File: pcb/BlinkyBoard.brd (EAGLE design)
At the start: 25.2 x 10 mm, 27 parts, among them Q1 16 MHz

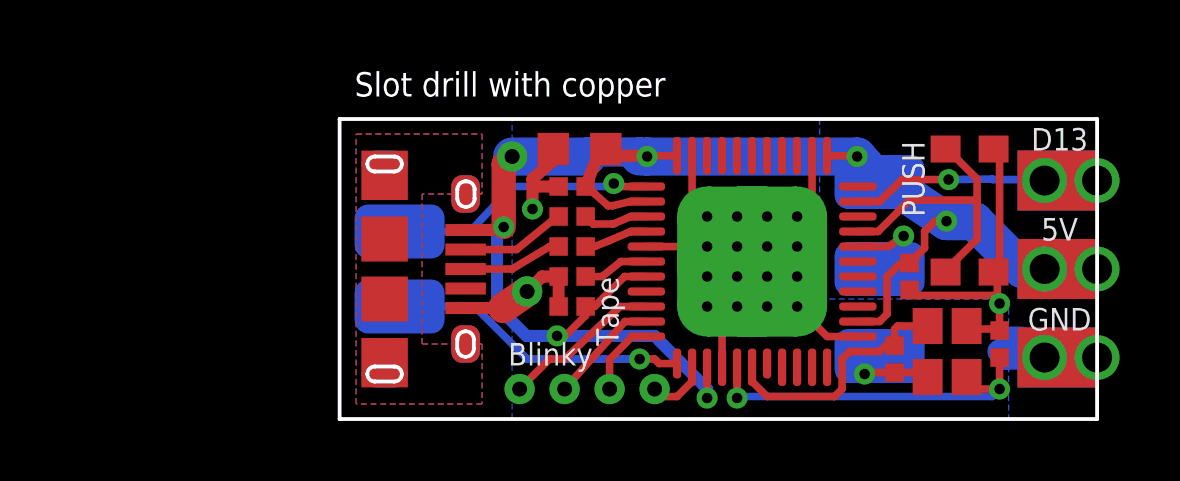
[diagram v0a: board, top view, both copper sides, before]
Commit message: RevF release: modify pads to support WS2811B
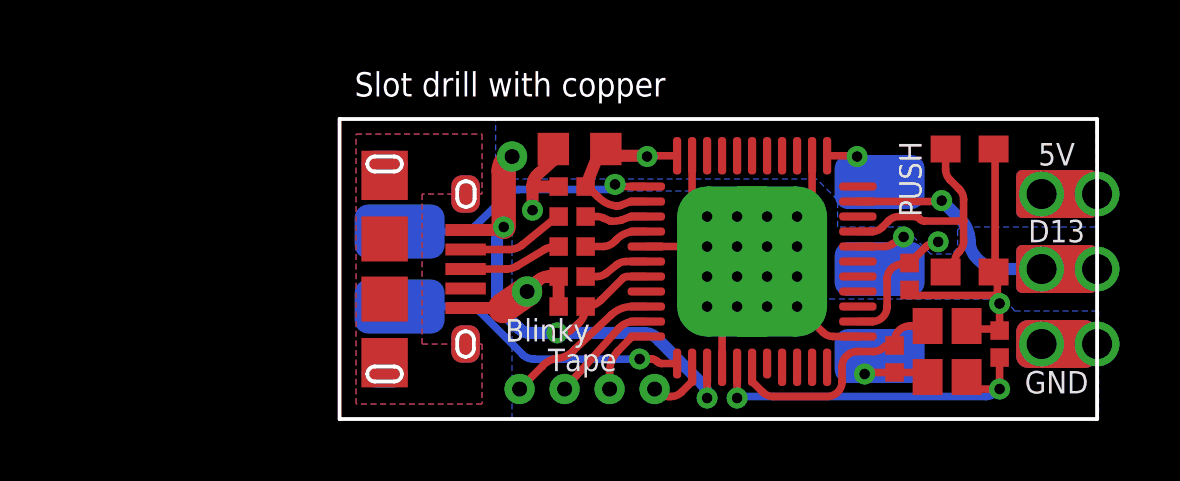
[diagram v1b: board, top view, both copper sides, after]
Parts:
- removed WS1, WS3: WS2811_CONNECTORSTRIP, blinkiverse:WS2811_CONNECTOR
- added U$9: WS2812B_CONNECTOR, blinkiverse:WS2812B_CONNECTOR
- moved U$15 0.36 mm to (20.9, 6.70)
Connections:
- net D13: now also U$9.DATA, U$9.DATA1, U$9.DATA_1, U$9.DATA_2; no longer WS1.DATA, WS3.DATA
- net GND: now also U$9.GND, U$9.GND1, U$9.GND_1, U$9.GND_2; no longer WS1.GND, WS3.GND
- net VCC: now also U$9.5V, U$9.5V1, U$9.5V_1, U$9.5V_2; no longer WS1.5V, WS3.5V
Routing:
- net VCC: track 54.6 -> 31.2 mm, vias 8 -> 6
- net GND: track 36.4 -> 31.6 mm, vias 5 -> 3
- net D10: track 9.68 -> 8.51 mm
- net D13: track 8.99 -> 9.69 mm, vias 3 -> 1
- net N$9: track 8.41 -> 7.81 mm
- added copper zone on layer 16, net VCC
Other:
- board text added: "8/2013"
- board text added: "Rev F"
- board text removed: "7/13"
- board text removed: "Rev E"

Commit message: Flip gnd/5v to match WS2812B strip.
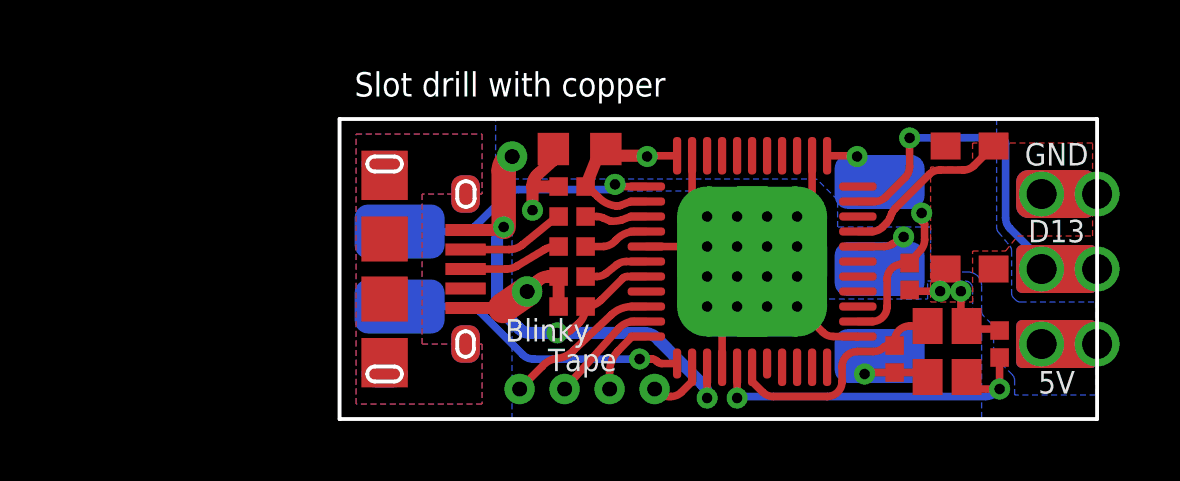
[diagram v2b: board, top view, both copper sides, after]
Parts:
- S1: device blinkyboard:GLOWBOARD_KMR211G_SWITCH -> blinkiverse:GLOWBOARD_KMR211G_SWITCH
- turned S1 to 90 degrees
- flipped U$9 to the bottom, turned to 180 degrees
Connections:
- net D10: no longer S1.P$3
- net GND: no longer S1.P$2
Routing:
- net GND: track 31.6 -> 24.7 mm, vias 3 -> 4
- net D13: track 9.69 -> 13.0 mm
- net D10: track 8.51 -> 5.69 mm
- net VCC: track 31.2 -> 31.9 mm
- added copper zone on layer 1, net GND
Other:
- board text added: "Rev G"
- board text removed: "PUSH"
- board text removed: "Rev F"

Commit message: Silkscreen fix: Analog is on A9, not A11!
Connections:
- net A10 renamed A9
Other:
- board text added: "A9"
- board text removed: "A11"
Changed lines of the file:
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@@
 <?xml version="1.0" encoding="utf-8"?>
 <!DOCTYPE eagle SYSTEM "eagle.dtd">
-<eagle version="6.5.0">
+<eagle version="6.4">
 <drawing>
 <settings>
@@
 <text x="23.9" y="5.89" size="0.75" layer="26" font="vector" ratio="15" rot="MR0" align="bottom-center">D13</text>
 <text x="23.9" y="8.45" size="0.75" layer="26" font="vector" ratio="15" rot="MR0" align="bottom-center">GND</text>
-<text x="20.5" y="8.75" size="0.75" layer="26" font="vector" ratio="15" rot="MR0" align="bottom-center">5V</text>
+<text x="20.3" y="8.75" size="0.75" layer="26" font="vector" ratio="15" rot="MR0" align="bottom-center">5V</text>
 <text x="20.75" y="2" size="0.75" layer="26" font="vector" ratio="15" rot="MR0" align="center">GND</text>
-<text x="20.5" y="8.75" size="0.75" layer="26" font="vector" ratio="15" rot="MR0" align="bottom-center">5V</text>
-<text x="20.75" y="5" size="0.75" layer="26" font="vector" ratio="15" rot="MR0" align="center">A11</text>
+<text x="20.35" y="5" size="0.75" layer="26" font="vector" ratio="15" rot="MR0" align="center">A9</text>
 <text x="4.35" y="6.25" size="0.75" layer="26" font="vector" ratio="15" rot="MR0" align="center">D7</text>
 <text x="4.65" y="3.75" size="0.75" layer="26" font="vector" ratio="15" rot="MR0" align="center">D11</text>
@@
 <wire x1="9.14" y1="7.75" x2="10.225" y2="7.75" width="0.254" layer="1"/>
 </signal>
-<signal name="A10">
+<signal name="A9">
 <contactref element="U$2" pad="29"/>
 <via x="18.8" y="6.07" extent="1-16" drill="0.35"/>
@@
 </signal>
 </signals>
-<errors>
-</errors>
 </board>
 </drawing>

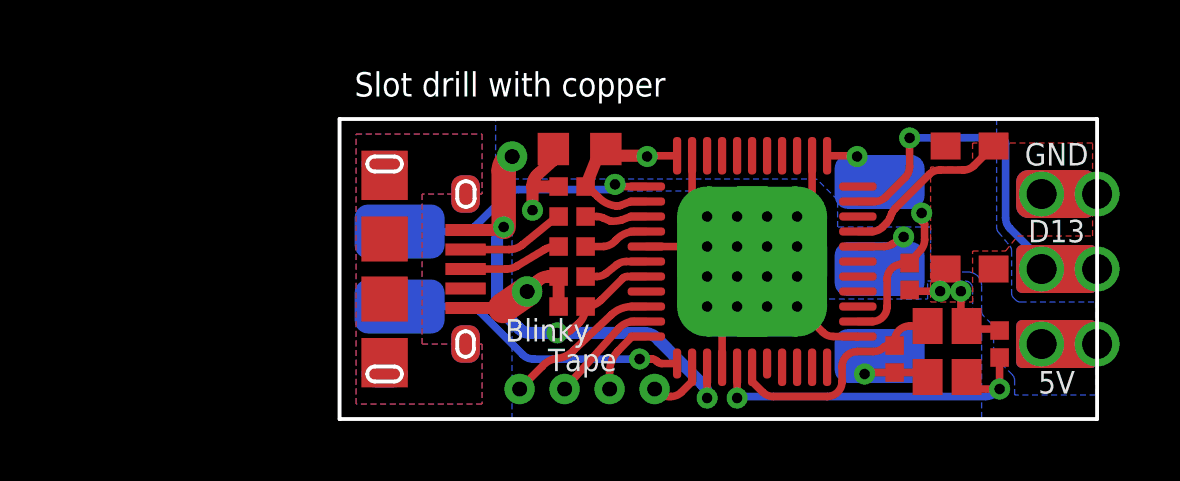
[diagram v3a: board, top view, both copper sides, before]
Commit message: Add series resistor to the output data line, so it can be removed from the flex strip
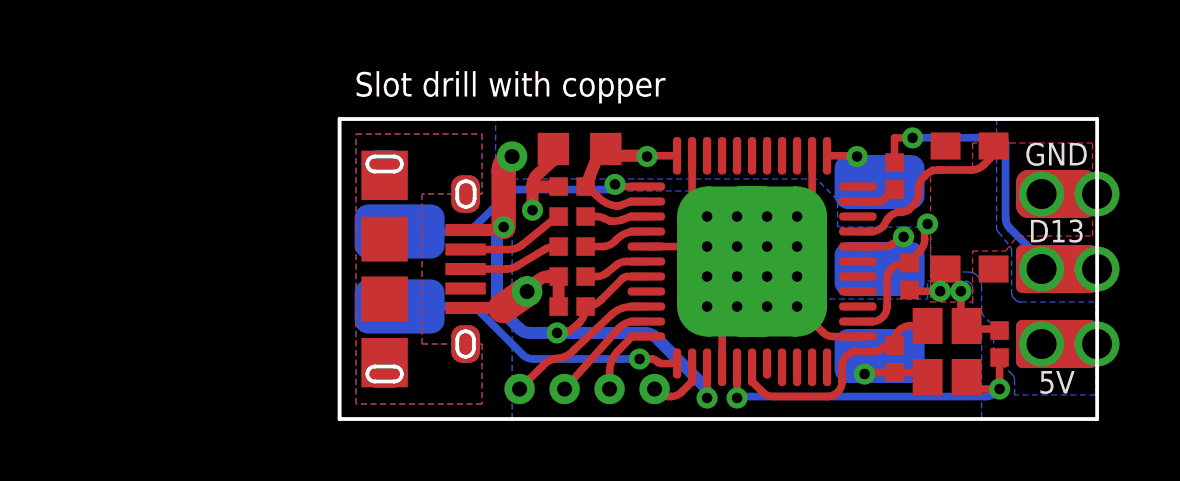
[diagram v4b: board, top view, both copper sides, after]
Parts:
- added R3: ??, blinkiverse:RES_0402_KEMET_MEDIAN
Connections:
- new net LED_DATA: R3.P$2, U$9.DATA, U$9.DATA1, U$9.DATA_1, U$9.DATA_2
- net D13: now also R3.P$1; no longer U$9.DATA, U$9.DATA1, U$9.DATA_1, U$9.DATA_2
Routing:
- net D13: track 13.0 -> 1.38 mm, vias 1 -> 0
- net LED_DATA: track 0.00 -> 10.8 mm, vias 0 -> 1
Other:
- board text added: "11/2013"
- board text added: "Rev H"
- board text added: "blinkinlabs.com"
- board text removed: "8/2013"
- board text removed: "Blinky"
- board text removed: "Rev G"
- board text removed: "Tape"
- board text removed: "blinkytape.com"
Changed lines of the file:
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@@
 <?xml version="1.0" encoding="utf-8"?>
 <!DOCTYPE eagle SYSTEM "eagle.dtd">
-<eagle version="6.4">
+<eagle version="6.5.0">
 <drawing>
 <settings>
@@
 <text x="9.15" y="6" size="1.016" layer="26" font="vector" ratio="20" rot="MR0" align="center">Blinky
 Tape</text>
-<text x="9.15" y="3.85" size="0.8128" layer="26" font="vector" ratio="20" rot="MR0" align="center">Rev G</text>
+<text x="9.15" y="3.85" size="0.8128" layer="26" font="vector" ratio="20" rot="MR0" align="center">Rev H</text>
 <text x="23.9" y="0.85" size="0.75" layer="25" font="vector" ratio="15" align="bottom-center">5V</text>
 <text x="23.9" y="5.89" size="0.75" layer="25" font="vector" ratio="15" align="bottom-center">D13</text>
 <text x="23.9" y="8.45" size="0.75" layer="25" font="vector" ratio="15" align="bottom-center">GND</text>
-<text x="8.09" y="1.97" size="0.75" layer="25" font="vector" ratio="15" align="center">Tape</text>
-<text x="11.24" y="2.6" size="0.9" layer="26" font="vector" ratio="20" rot="MR0" align="center">blinkytape.com</text>
+<text x="11.24" y="2.6" size="0.9" layer="26" font="vector" ratio="20" rot="MR0" align="center">blinkinlabs.com</text>
 <text x="23.9" y="0.85" size="0.75" layer="26" font="vector" ratio="15" rot="MR0" align="bottom-center">5V</text>
 <text x="23.9" y="5.89" size="0.75" layer="26" font="vector" ratio="15" rot="MR0" align="bottom-center">D13</text>
@@
 <text x="4.65" y="3.75" size="0.75" layer="26" font="vector" ratio="15" rot="MR0" align="center">D11</text>
 <text x="0.5" y="10.75" size="0.8128" layer="46">Slot drill with copper</text>
-<text x="13.75" y="8.75" size="0.75" layer="26" font="vector" ratio="15" rot="MR0" align="center">8/2013</text>
-<text x="6.93" y="2.96" size="0.75" layer="25" font="vector" ratio="15" align="center">Blinky</text>
+<text x="13.75" y="8.75" size="0.75" layer="26" font="vector" ratio="15" rot="MR0" align="center">11/2013</text>
 </plain>
 <attributes>
@@
 <element name="U$15" library="blinkiverse" package="OSHW-LOGO-S" value="" x="20.89" y="6.7" rot="MR0"/>
 <element name="U$9" library="blinkiverse" package="WS2812B_CONNECTOR" value="WS2812B_CONNECTOR" x="23.9" y="5" rot="MR180"/>
+<element name="R3" library="blinkiverse" package="RES_0402_KEMET_MEDIAN" value="??" x="18.5" y="8.1" rot="R90"/>
 </elements>
 <signals>
@@
 <contactref element="S1" pad="P$4"/>
 <contactref element="U$2" pad="30"/>
-<wire x1="17.275" y1="6.25" x2="17.74289375" y2="6.25" width="0.254" layer="1"/>
-<wire x1="17.74289375" y1="6.25" x2="18.096446875" y2="6.396446875" width="0.254" layer="1" curve="45"/>
-<wire x1="18.4033625" y1="6.8495375" x2="18.338059375" y2="6.691884375" width="0.254" layer="1"/>
-<wire x1="18.338059375" y1="6.691884375" x2="18.229675" y2="6.529675" width="0.254" layer="1" curve="-22.499569"/>
-<wire x1="18.229675" y1="6.529675" x2="18.096446875" y2="6.396446875" width="0.254" layer="1"/>
-<wire x1="19.653553125" y1="8.153553125" x2="18.511746875" y2="7.011746875" width="0.254" layer="1"/>
-<wire x1="18.511746875" y1="7.011746875" x2="18.4033625" y2="6.8495375" width="0.254" layer="1" curve="22.499685"/>
-<wire x1="19.653553125" y1="8.153553125" x2="20.00710625" y2="8.3" width="0.254" layer="1" curve="-45"/>
-<wire x1="20.00710625" y1="8.3" x2="20.79289375" y2="8.3" width="0.254" layer="1"/>
-<wire x1="20.79289375" y1="8.3" x2="21.146446875" y2="8.446446875" width="0.254" layer="1" curve="45"/>
-<wire x1="21.146446875" y1="8.446446875" x2="21.8" y2="9.1" width="0.254" layer="1"/>
+<wire x1="17.275" y1="6.25" x2="17.701471875" y2="6.25" width="0.254" layer="1"/>
+<wire x1="17.701471875" y1="6.25" x2="18.125734375" y2="6.425734375" width="0.254" layer="1" curve="44.999789"/>
+<wire x1="18.125734375" y1="6.425734375" x2="18.263603125" y2="6.663603125" width="0.254" layer="1"/>
+<wire x1="18.263603125" y1="6.663603125" x2="18.651471875" y2="6.9" width="0.254" layer="1" curve="-45"/>
+<wire x1="18.651471875" y1="6.9" x2="18.975734375" y2="6.975734375" width="0.254" layer="1" curve="44.999789"/>
+<wire x1="18.975734375" y1="6.975734375" x2="19.124265625" y2="7.124265625" width="0.254" layer="1"/>
+<wire x1="19.124265625" y1="7.124265625" x2="19.3" y2="7.548528125" width="0.254" layer="1" curve="44.999702"/>
+<wire x1="19.3" y1="7.548528125" x2="19.3" y2="7.651471875" width="0.254" layer="1"/>
+<wire x1="19.3" y1="7.651471875" x2="19.475734375" y2="8.075734375" width="0.254" layer="1" curve="-44.999789"/>
+<wire x1="19.475734375" y1="8.075734375" x2="19.524265625" y2="8.124265625" width="0.254" layer="1"/>
+<wire x1="19.524265625" y1="8.124265625" x2="19.948528125" y2="8.3" width="0.254" layer="1" curve="-44.999702"/>
+<wire x1="19.948528125" y1="8.3" x2="21.051471875" y2="8.3" width="0.254" layer="1"/>
+<wire x1="21.051471875" y1="8.3" x2="21.475734375" y2="8.475734375" width="0.254" layer="1" curve="44.999789"/>
+<wire x1="21.475734375" y1="8.475734375" x2="21.8" y2="8.8" width="0.254" layer="1"/>
+<wire x1="21.8" y1="8.8" x2="21.8" y2="9.1" width="0.254" layer="1"/>
 </signal>
 <signal name="AREF">
@@
 <wire x1="9.550390625" y1="5.25" x2="10.225" y2="5.25" width="0.254" layer="1"/>
 </signal>
-<signal name="D13">
-<contactref element="U$2" pad="32"/>
+<signal name="LED_DATA">
+<via x="19.1" y="9.37" extent="1-16" drill="0.35"/>
+<wire x1="19.1" y1="9.37" x2="22" y2="9.38" width="0.254" layer="16"/>
+<wire x1="22" y1="9.38" x2="22.2" y2="9.18" width="0.254" layer="16" curve="-90"/>
+<wire x1="22.2" y1="9.18" x2="22.2" y2="6.70710625" width="0.254" layer="16"/>
+<wire x1="22.2" y1="6.70710625" x2="22.346446875" y2="6.353553125" width="0.254" layer="16" curve="45"/>
+<wire x1="22.346446875" y1="6.353553125" x2="23.4" y2="5.3" width="0.254" layer="16"/>
 <contactref element="U$9" pad="DATA1"/>
 <contactref element="U$9" pad="DATA_1"/>
 <contactref element="U$9" pad="DATA_2"/>
 <contactref element="U$9" pad="DATA"/>
+<contactref element="R3" pad="P$2"/>
 <wire x1="25.25" y1="5" x2="23.9" y2="5" width="0.4064" layer="16"/>
 <wire x1="23.4" y1="5" x2="23.9" y2="5" width="0.4064" layer="16"/>
-<wire x1="17.275" y1="7.25" x2="17.84289375" y2="7.25" width="0.254" layer="1"/>
-<wire x1="17.84289375" y1="7.25" x2="18.196446875" y2="7.396446875" width="0.254" layer="1" curve="45"/>
-<wire x1="18.196446875" y1="7.396446875" x2="18.853553125" y2="8.053553125" width="0.254" layer="1"/>
-<wire x1="18.853553125" y1="8.053553125" x2="19" y2="8.40710625" width="0.254" layer="1" curve="45"/>
-<wire x1="19" y1="8.40710625" x2="19" y2="9.37" width="0.254" layer="1"/>
-<via x="19" y="9.37" extent="1-16" drill="0.35"/>
-<wire x1="19" y1="9.37" x2="22" y2="9.38" width="0.254" layer="16"/>
-<wire x1="22" y1="9.38" x2="22.2" y2="9.18" width="0.254" layer="16" curve="-90"/>
-<wire x1="22.2" y1="9.18" x2="22.2" y2="6.70710625" width="0.254" layer="16"/>
-<wire x1="22.2" y1="6.70710625" x2="22.346446875" y2="6.353553125" width="0.254" layer="16" curve="45"/>
-<wire x1="22.346446875" y1="6.353553125" x2="23.4" y2="5.3" width="0.254" layer="16"/>
-<wire x1="23.4" y1="5.3" x2="23.4" y2="5" width="0.254" layer="16"/>
+<wire x1="19.1" y1="9.37" x2="18.5" y2="9.37" width="0.254" layer="1"/>
+<wire x1="18.5" y1="9.37" x2="18.5" y2="8.55" width="0.254" layer="1"/>
 <wire x1="23.9" y1="5" x2="23.9" y2="5" width="0" layer="19" extent="1-16"/>
+<wire x1="23.4" y1="5.3" x2="23.4" y2="5" width="0" layer="19" extent="16-16"/>
 </signal>
 <signal name="VCC">
@@
 <wire x1="5.05" y1="6.3" x2="5.47" y2="6.4" width="0.4" layer="1"/>
 <contactref element="U$12" pad="P$1"/>
-<via x="19.40076875" y="6.866153125" extent="1-16" drill="0.35"/>
+<via x="19.6" y="6.5" extent="1-16" drill="0.35"/>
 <wire x1="8.2" y1="3.75" x2="7.984815625" y2="3.200965625" width="0.254" layer="1" curve="-45.83031"/>
 <wire x1="7.984815625" y1="3.200965625" x2="7.67931875" y2="2.944196875" width="0.254" layer="1"/>
@@
 <wire x1="19.38198125" y1="5.65063125" x2="19.50056875" y2="5.975284375" width="0.254" layer="1" curve="40.441105"/>
 <wire x1="19.50056875" y1="5.975284375" x2="19.5" y2="6.5" width="0.254" layer="1"/>
-<wire x1="19.5" y1="6.5" x2="19.40076875" y2="6.59923125" width="0.254" layer="1"/>
-<wire x1="19.40076875" y1="6.59923125" x2="19.40076875" y2="6.866153125" width="0.254" layer="1"/>
+<wire x1="19.6" y1="6.5" x2="19.5" y2="6.5" width="0.254" layer="1"/>
 <wire x1="23.9" y1="2.5" x2="23.9" y2="2.5" width="0" layer="19" extent="1-16"/>
 </signal>
@@
 <wire x1="4.2" y1="7.5" x2="4.2" y2="7.5" width="0" layer="19" extent="1-16"/>
 </signal>
+<signal name="D13">
+<contactref element="U$2" pad="32"/>
+<contactref element="R3" pad="P$1"/>
+<wire x1="17.275" y1="7.25" x2="18.05" y2="7.25" width="0.254" layer="1"/>
+<wire x1="18.05" y1="7.25" x2="18.5" y2="7.65" width="0.254" layer="1"/>
+</signal>
 </signals>

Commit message: RevI PCB, improved component spacing and power routing
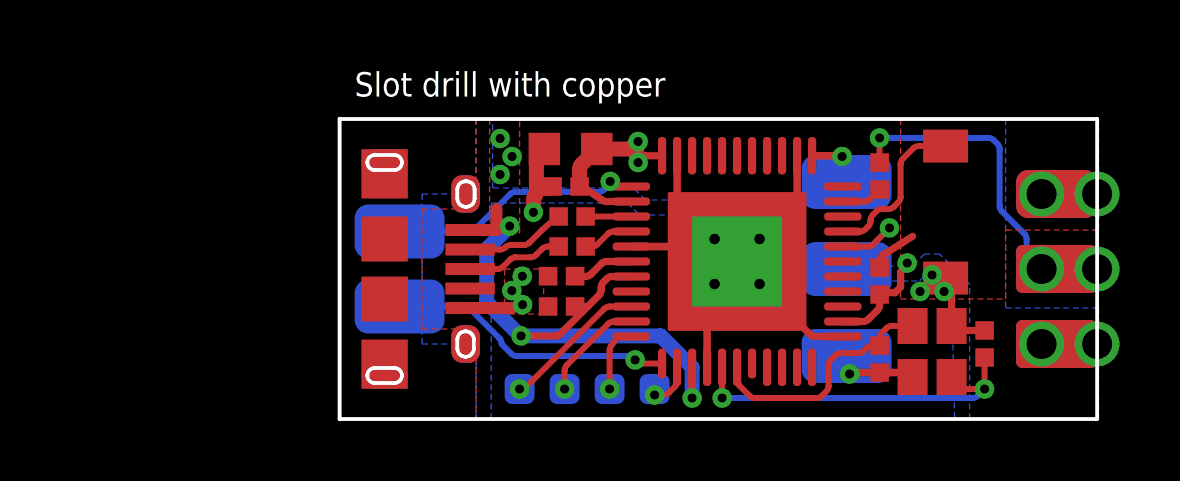
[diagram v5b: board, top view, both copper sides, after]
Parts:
- removed S1: Normally open, blinkiverse:GLOWBOARD_KMR211G_SWITCH
- removed U$8: TEST_VIA, blinkiverse:TEST_VIA_.5MM
- Q1: device blinkiverse:CRSYTAL_2520 -> blinkinlabs:CRSYTAL_2520
- U$1, U$3, U$5, U$6: value TEST_VIA -> TEST_PAD_SMT; device blinkiverse:TEST_VIA_.5MM -> blinkinlabs:TEST_PAD_1MM
- U$2: value ARDUINO_LEONARDO-REV3B_SMARTPRJ_ATMEGA32U4-XUMU_MODDED -> ATMEGA32U4MU_MODDED; device blinkiverse:QFN44ML_7X7_LONGLEADS_MOD -> blinkinlabs:QFN44ML_7X7_LONGLEADS_MOD
- U$4: value MICRO_USBSMT+THRUHULE -> USB_MICROSMT+THRUHULE; device blinkiverse:MICRO_USB_FCI_THRUHOLE -> blinkinlabs:USB_MICRO_THRUHOLE
- U$7: value TEST_VIA -> (none); device blinkiverse:TEST_VIA_.5MM -> blinkinlabs:BUTTON_2P_SMD
- moved U$7 14.2 mm to (20.2, 6.90), turned to 270 degrees
- moved U$15 7.73 mm to (13.3, 8.10)
- moved U$11 1.10 mm to (16.9, 5.00)
- moved U$12 1.10 mm to (16.9, 7.90)
- moved U$13 1.10 mm to (16.9, 2.10)
- moved C4 1.01 mm to (18.0, 4.60), turned to 90 degrees
- moved C6 0.50 mm to (21.5, 2.50)
- moved C7 0.50 mm to (18.0, 2.00)
- moved Q1 0.50 mm to (19.8, 2.25)
- moved R3 0.50 mm to (18.0, 8.10)
- moved U$2 0.50 mm to (13.2, 5.25)
- moved C5 0.35 mm to (7.40, 4.76)
- moved C3 0.35 mm to (7.40, 3.75)
- moved C1 0.30 mm to (7.70, 9.00)
- moved C2 0.20 mm to (7.55, 7.75)
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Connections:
- net D10: now also U$7.P$3; no longer S1.P$4
- net GND: now also U$7.P$4; no longer S1.P$1, U$2.PAD@10, U$2.PAD@11, U$2.PAD@12, U$2.PAD@14, U$2.PAD@15, U$2.PAD@2, U$2.PAD@3, U$2.PAD@5, U$2.PAD@6, U$2.PAD@7, U$2.PAD@8, U$2.PAD@9, U$7.P$1
- net VCC: no longer U$8.P$1
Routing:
- net GND: track 24.7 -> 19.5 mm, vias 4 -> 8
- net VCC: track 31.6 -> 30.5 mm, vias 6 -> 10
- net LED_DATA: track 10.8 -> 11.7 mm
- net A9: track 2.97 -> 3.80 mm
- net D10: track 6.03 -> 5.38 mm
- net D-: track 2.07 -> 1.53 mm
- net D7: track 8.98 -> 8.44 mm
- net SCK: track 5.19 -> 4.85 mm, vias 0 -> 1
- net RST: track 1.97 -> 1.64 mm, vias 0 -> 1
- net MISO: track 2.47 -> 2.28 mm, vias 0 -> 1
- net MOSI: track 3.68 -> 3.55 mm, vias 0 -> 1
- added copper zone on layer 1, net VCC
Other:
- board text added: "/Users/matt/Blinkinlabs-Projects/BlinkyTape/pcb/Untitled.BMP"
- board text added: "2015/02"
- board text added: "Rev I"
- board text removed: "11/2013"
- board text removed: "Rev H"
